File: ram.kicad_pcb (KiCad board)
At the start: 2 copper layers, 116.8 x 52.8 mm, 10 parts, among them U1 74AHCT1G00, U3 74AHCT1G00

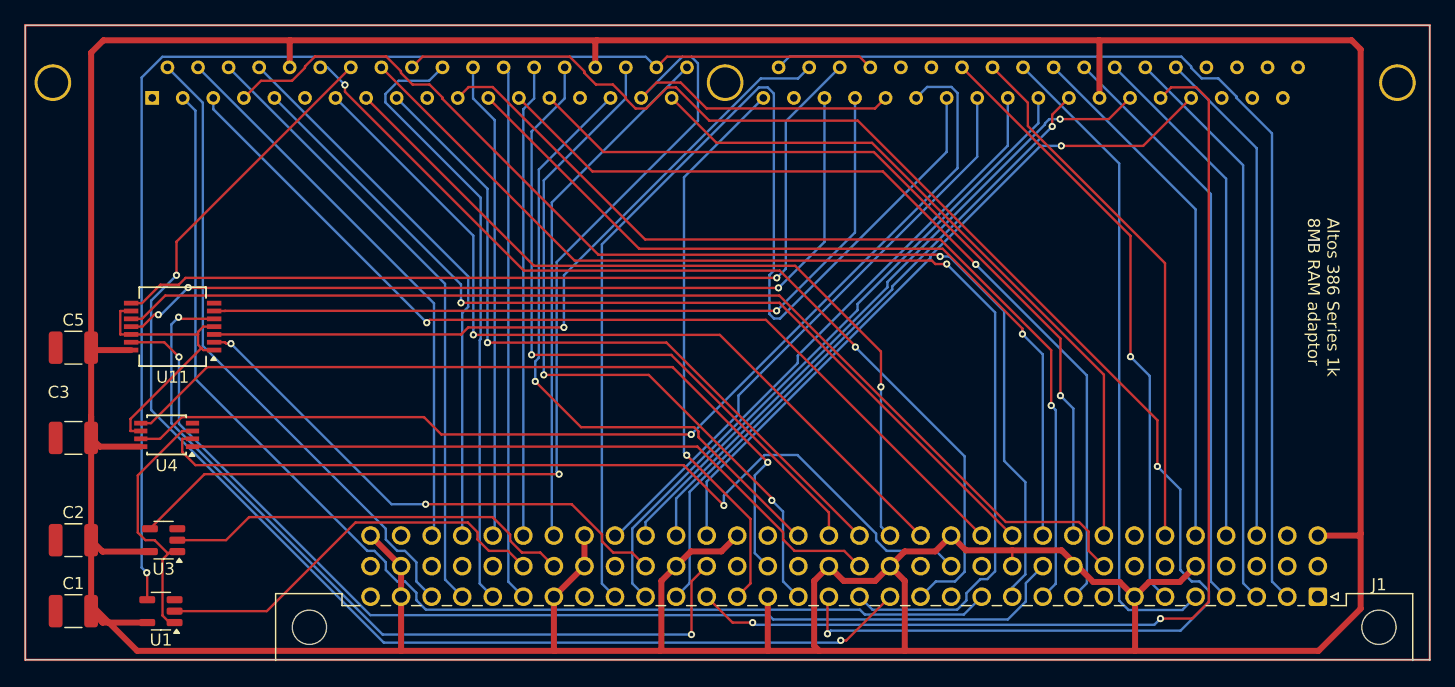
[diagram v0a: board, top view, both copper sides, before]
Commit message: Made a 4 layer PCB, and also smaller, routing done.
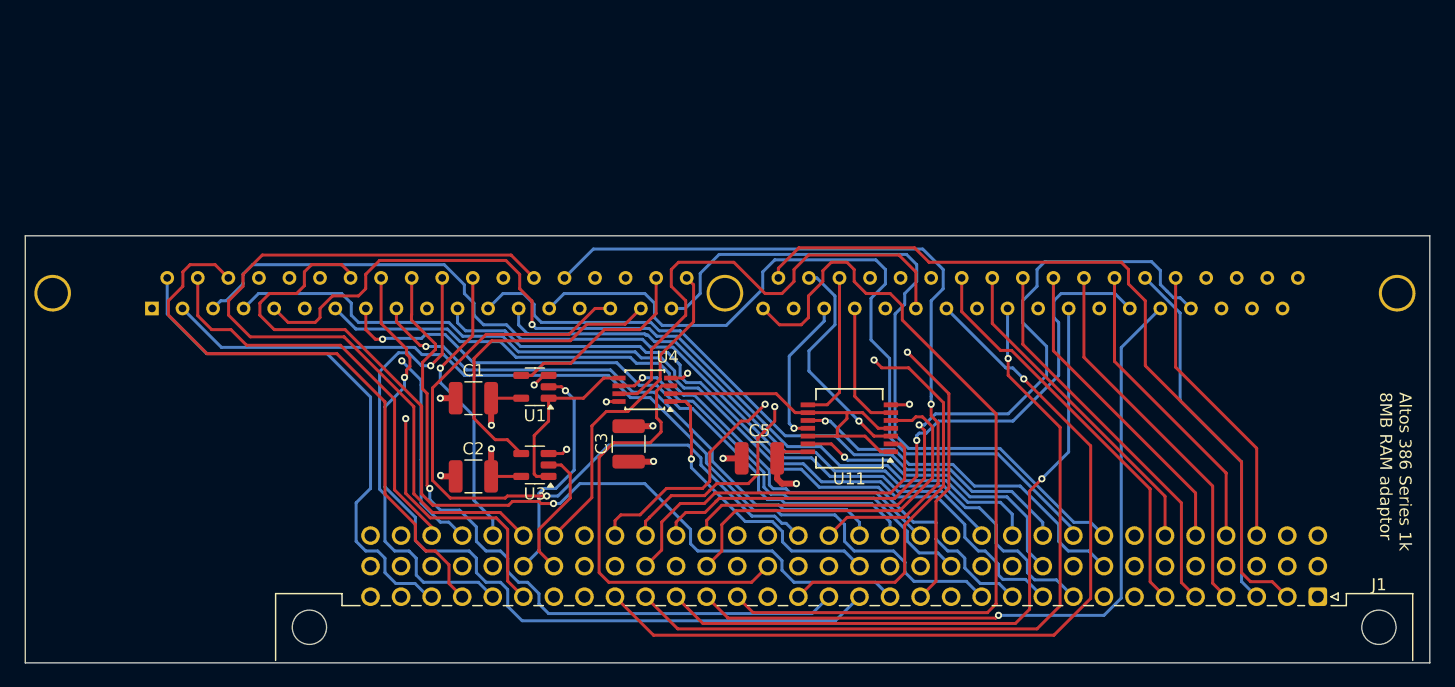
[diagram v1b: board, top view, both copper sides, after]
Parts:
- moved C5 57.8 mm to (80.5, 163.5)
- moved U11 56.9 mm to (88.0, 161.0)
- moved C3 46.2 mm to (69.7, 162.3), turned to 90 degrees
- moved U4 39.9 mm to (71.0, 157.8)
- moved C1 37.7 mm to (56.8, 158.5)
- moved U1 36.3 mm to (61.9, 157.6)
- moved C2 33.7 mm to (56.8, 165.0)
- moved U3 31.5 mm to (61.9, 164.1)
- moved U13 17.5 mm to (77.7, 149.8)
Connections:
- C1 pad 2: Net-(U1-VCC) -> VCC
- C2 pad 2: Net-(U3-VCC) -> VCC
- U1 pad 5: Net-(U1-VCC) -> VCC
- U3 pad 5: Net-(U3-VCC) -> VCC
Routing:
- net VCC: track 436.9 -> 19.0 mm, vias 0 -> 5
- net ~{RAS0}: track 106.0 -> 35.4 mm, vias 1 -> 0
- net A06: track 129.7 -> 59.5 mm, vias 2 -> 1
- net CAS2: track 91.3 -> 25.4 mm
- net ~{CAS3}: track 74.2 -> 12.6 mm, vias 1 -> 0
- net CAS3: track 91.9 -> 30.4 mm, vias 0 -> 1
- net ~{CAS2}: track 72.5 -> 12.5 mm, vias 3 -> 1
- net ~{CAS1}: track 67.2 -> 10.9 mm, vias 1 -> 0
- net ~{RAS1}: track 103.5 -> 50.3 mm, vias 1 -> 0
- net ~{RAS_OE}: track 66.9 -> 14.6 mm, vias 1 -> 0
- net ~{WE}: track 88.7 -> 41.2 mm, vias 1 -> 0
- net ~{CAS_OE}: track 74.1 -> 29.2 mm, vias 1 -> 0
- net ~{CAS0}: track 61.2 -> 19.0 mm
- net CAS1: track 68.8 -> 31.3 mm, vias 2 -> 0
- net WE: track 59.9 -> 24.8 mm, vias 0 -> 1
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- added copper zone on In1.Cu, net GND
- added copper zone on In2.Cu, net VCC
- removed copper zone on B.Cu, net GND
- removed copper zone on F.Cu, net GND
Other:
- board size 116.8 x 52.8 mm -> 116.8 x 35.5 mm
- copper layers 2 -> 4

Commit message: Add ICs descriptions
Cook first PCB iteration.
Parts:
- C3, C5: value C -> 0.1uF
- U1, U3: value 74AHCT1G00 -> SN74AHCT1G00DBVR
- U11: value ~ -> SN74AHCT00DR
- U4: value ~ -> 74AHCT3G04DC
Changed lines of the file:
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@@
 			)
 		)
-		(property "Value" "C"
+		(property "Value" "0.1uF"
 			(at 0 2.3 0)
 			(layer "F.Fab")
@@
 			)
 		)
-		(property "Value" "C"
+		(property "Value" "0.1uF"
 			(at 0 2.3 90)
 			(layer "F.Fab")
@@
 			)
 		)
-		(property "Value" "~"
+		(property "Value" "74AHCT3G04DC"
 			(at 0 2.55 0)
 			(layer "F.Fab")
@@
 			)
 		)
-		(property "Description" ""
+		(property "Description" "74AHCT3G04DC"
 			(at 0 0 180)
 			(unlocked yes)
@@
 			)
 		)
+		(property "LCSC" "C7622"
+			(at 0 0 180)
+			(unlocked yes)
+			(layer "F.Fab")
+			(hide yes)
+			(effects
+				(font
+					(size 1 1)
+					(thickness 0.15)
+				)
+			)
+		)
 		(sheetname "Root")
 		(sheetfile "ram.kicad_sch")
@@
 			)
 		)
-		(property "Value" "~"
+		(property "Value" "SN74AHCT00DR"
 			(at 0 4.2 0)
 			(layer "F.Fab")
@@
 			)
 		)
-		(property "Description" ""
+		(property "Description" "SN74AHCT00DR"
 			(at 0 0 180)
 			(unlocked yes)
@@
 			)
 		)
+		(property "LCSC" "C155451"
+			(at 0 0 180)
+			(unlocked yes)
+			(layer "F.Fab")
+			(hide yes)
+			(effects
+				(font
+					(size 1 1)
+					(thickness 0.15)
+				)
+			)
+		)
 		(sheetname "Root")
 		(sheetfile "ram.kicad_sch")
@@
 			)
 		)
-		(property "Value" "74AHCT1G00"
+		(property "Value" "SN74AHCT1G00DBVR"
 			(at 0 2.4 0)
 			(layer "F.Fab")
@@
 			)
 		)
+		(property "LCSC" "C473380"
+			(at 0 0 180)
+			(unlocked yes)
+			(layer "F.Fab")
+			(hide yes)
+			(effects
+				(font
+					(size 1 1)
+					(thickness 0.15)
+				)
+			)
+		)
 		(property ki_fp_filters "SOT* SG-*")
 		(sheetname "Root")
@@
 			(net 1 "VCC")
 			(pinfunction "Pin_c1")
-			(pintype "passive")
+			(pintype "power_in")
 		)
 		(pad "c2" thru_hole circle
@@
 			)
 		)
-		(property "Value" "74AHCT1G00"
+		(property "Value" "SN74AHCT1G00DBVR"
 			(at 0 2.4 0)
 			(layer "F.Fab")
@@
 					(thickness 0.15)
 				)
+			)
+		)
+		(property "LCSC" "C473380"
+			(at 0 0 180)
+			(unlocked yes)
+			(layer "F.Fab")
+			(hide yes)
+			(effects
+				(font
+					(size 1 1)
+					(thickness 0.15)
+				)

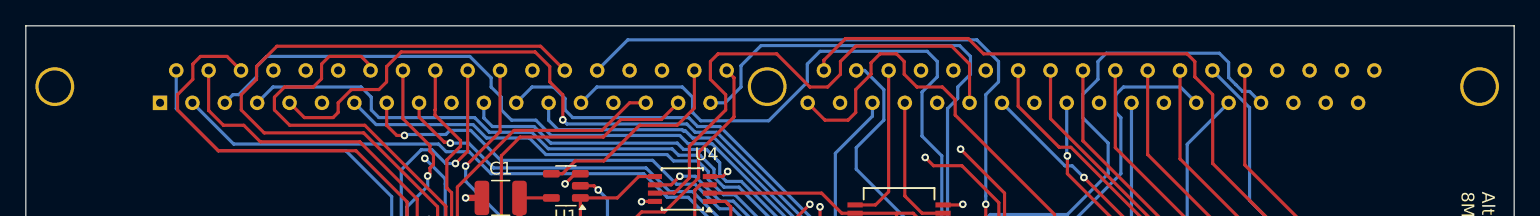
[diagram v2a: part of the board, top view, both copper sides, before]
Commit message: Fix simm position
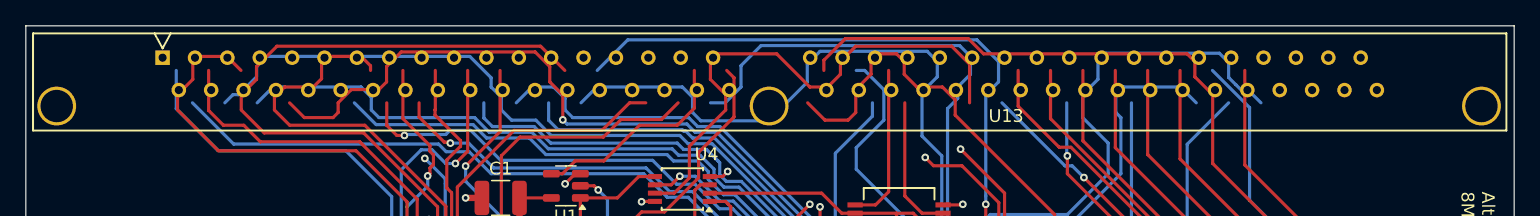
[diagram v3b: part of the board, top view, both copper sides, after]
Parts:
- U13: moved to F.Cu
- moved U13 0.20 mm to (77.9, 149.8), turned to 0 degrees
